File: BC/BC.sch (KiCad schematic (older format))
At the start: 32 parts, among them CON1 BARREL_JACK, Q1 Q_NMOS_GSD, Q10 Q_PMOS_GSD, Q11 Q_PMOS_GSD, Q12 Q_PMOS_GSD, Q13 Q_PMOS_GSD, Q14 Q_PMOS_GSD, Q15 Q_PMOS_GSD, Q16 Q_PMOS_GSD, Q2 Q_NMOS_GSD, Q3 Q_PMOS_GSD, Q4 Q_PMOS_GSD, Q5 Q_NMOS_GSD, Q6 Q_PMOS_GSD, Q7 Q_PMOS_GSD, Q8 Q_PMOS_GSD, Q9 Q_PMOS_GSD, SW1 SW_PUSH, U1 DS3231N, U2 MSP430G2203IPW28, U3 AP1117

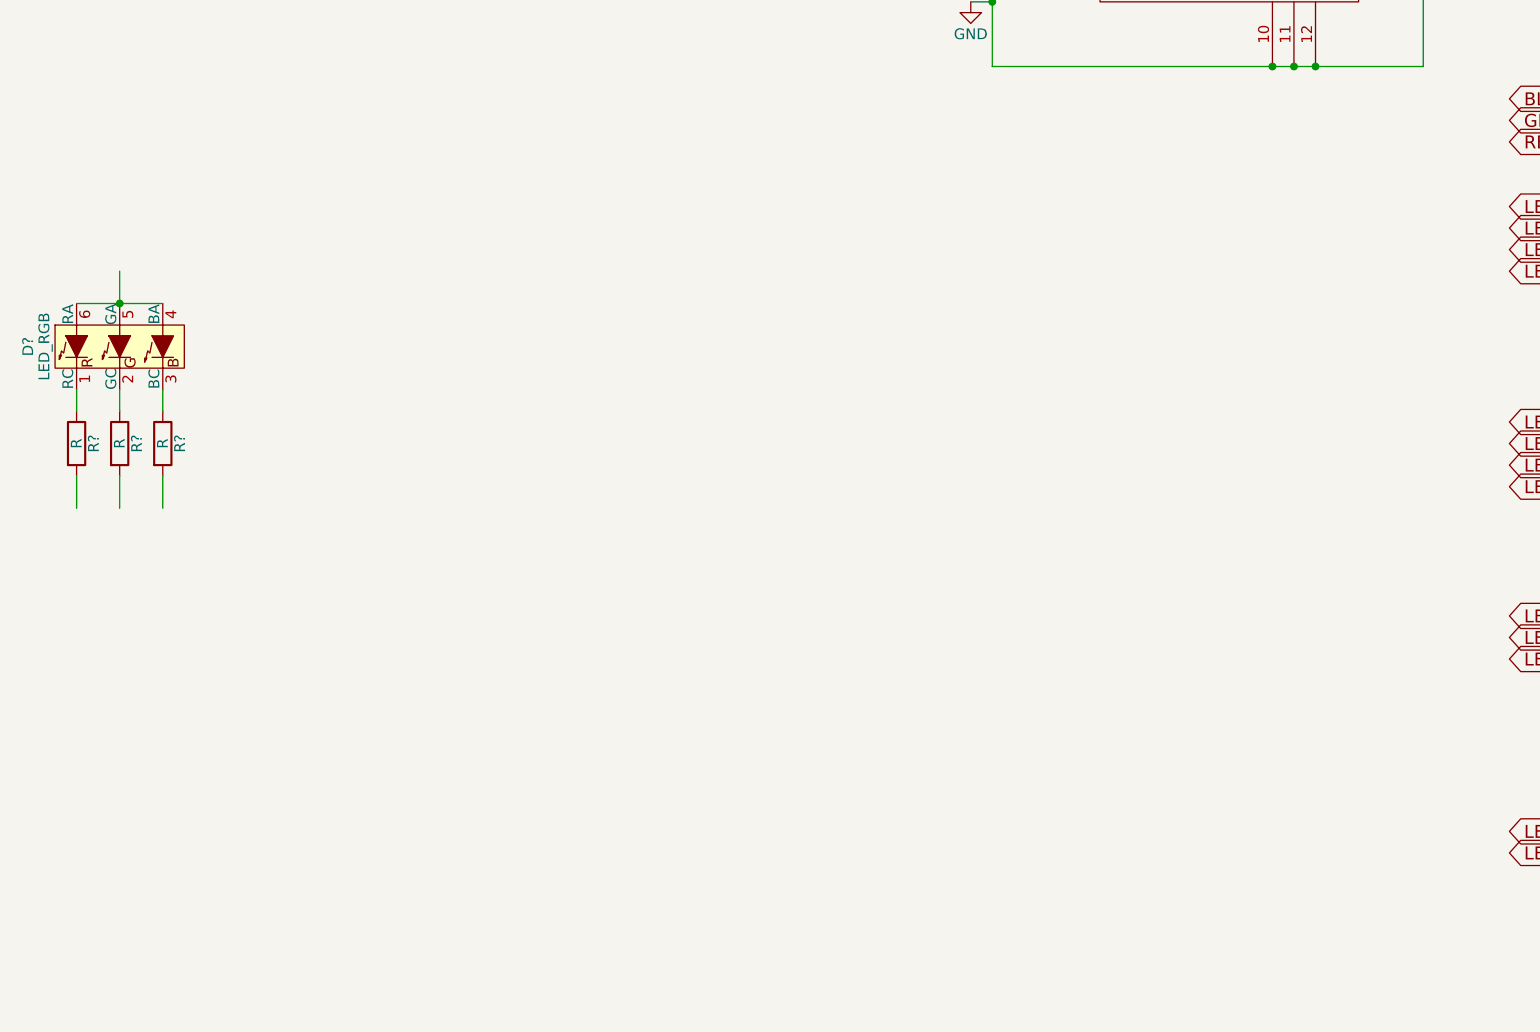
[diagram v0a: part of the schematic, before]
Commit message: Updated for 6pin RGB LED
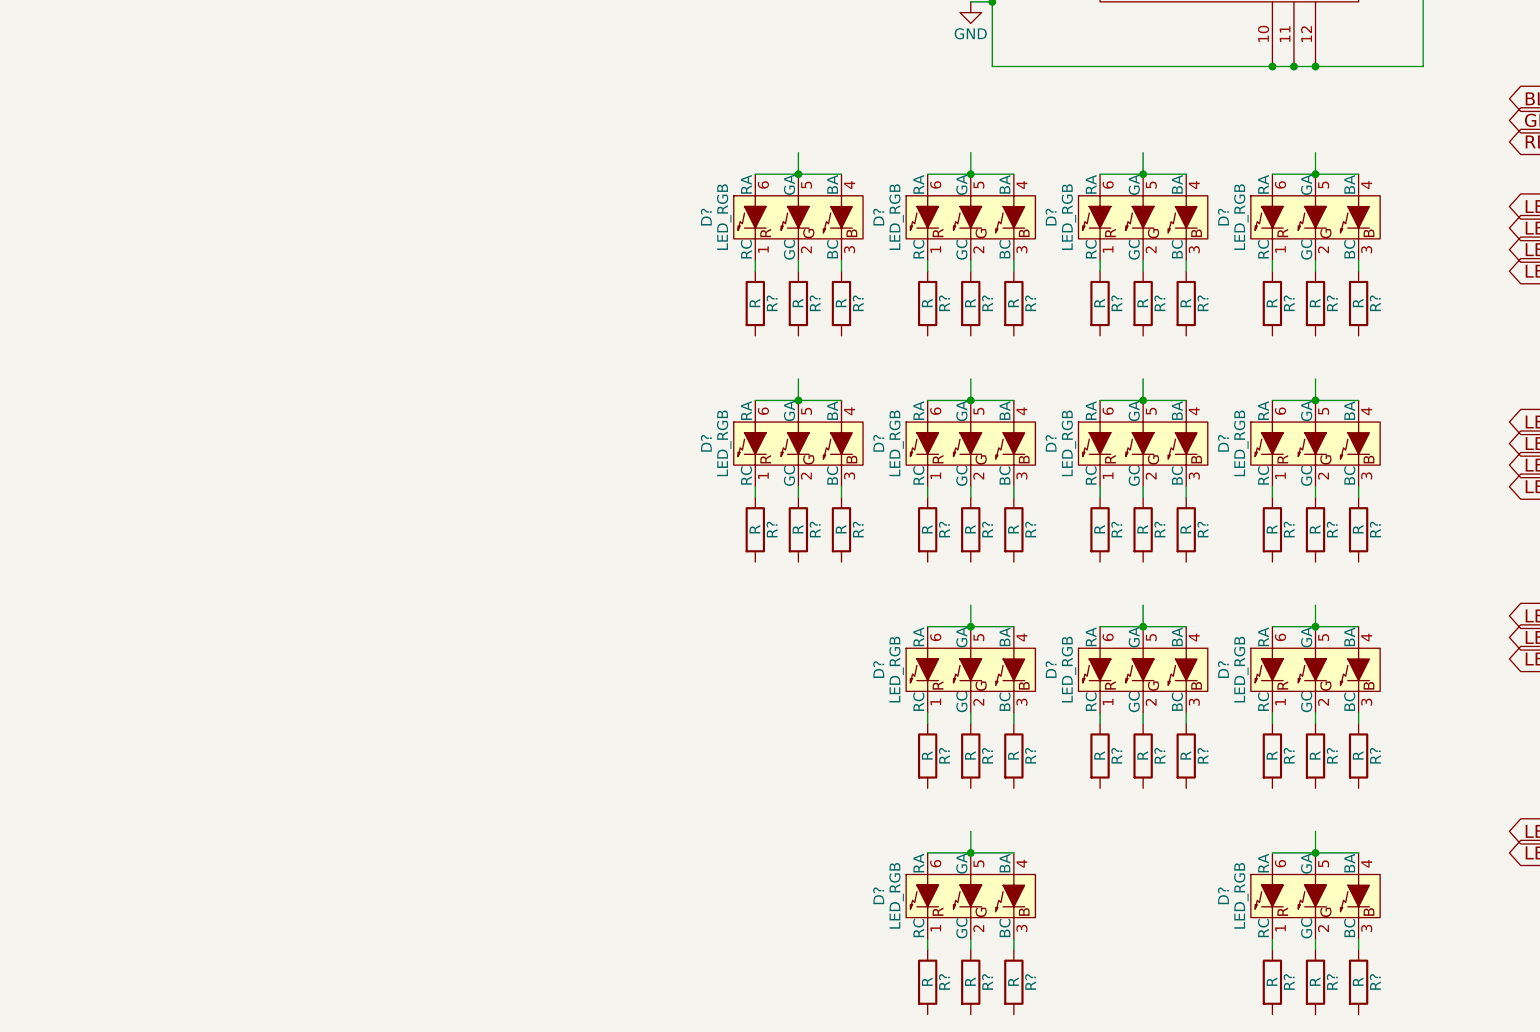
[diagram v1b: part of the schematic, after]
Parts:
- added D? (x12): LED_RGB, symbol LED_RGB
- added R? (x36): R, symbol R
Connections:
- wire segments 63 -> 120
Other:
- moved on the sheet: D?, R?

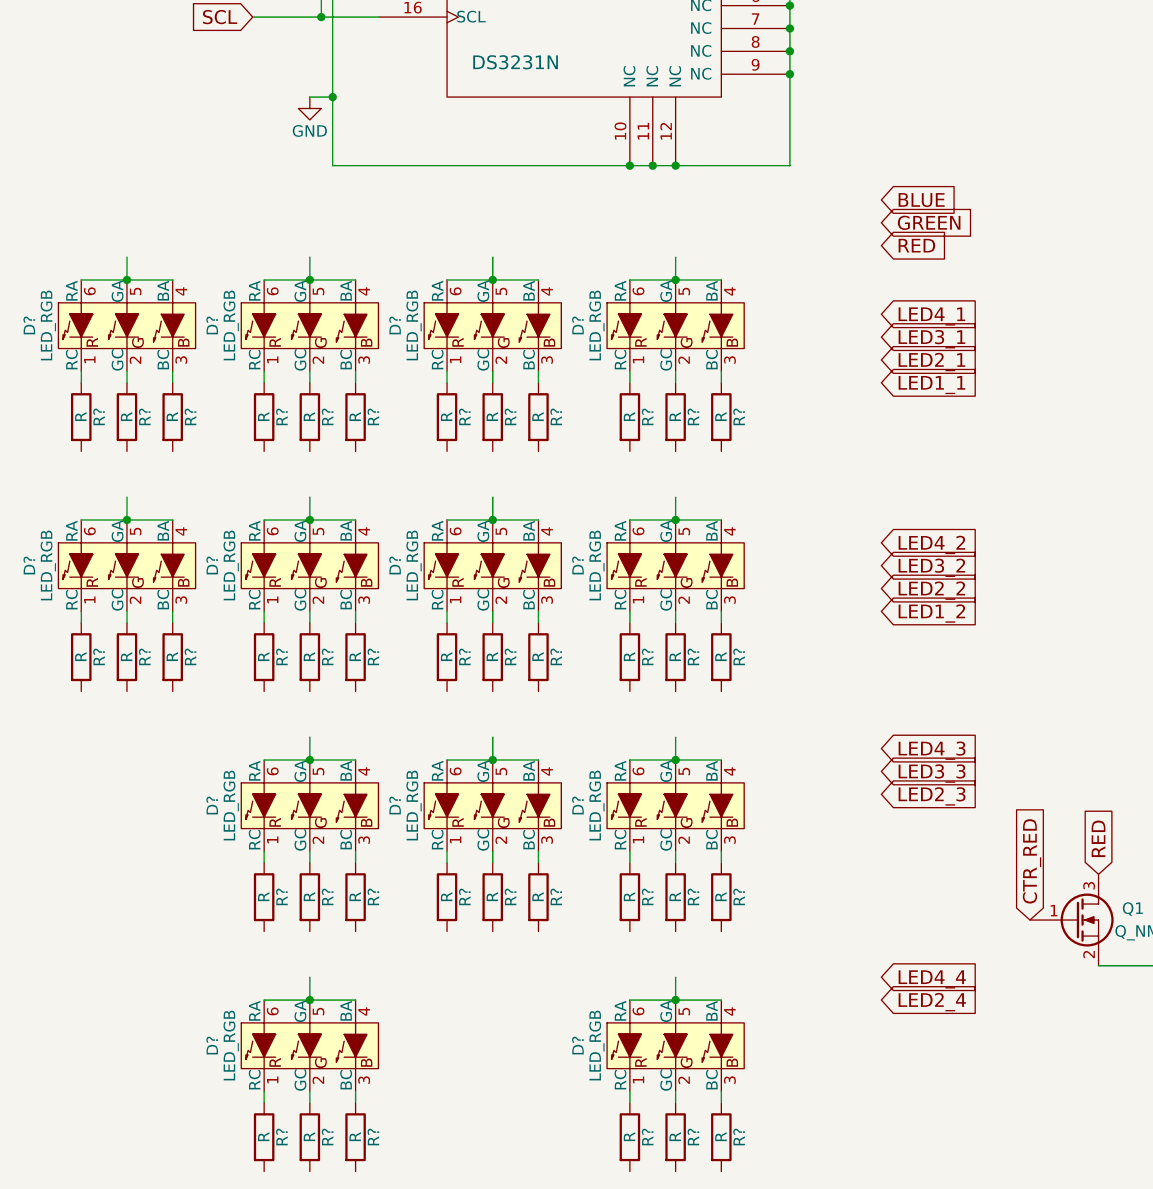
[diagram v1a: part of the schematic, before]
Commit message: Began PCB Layout
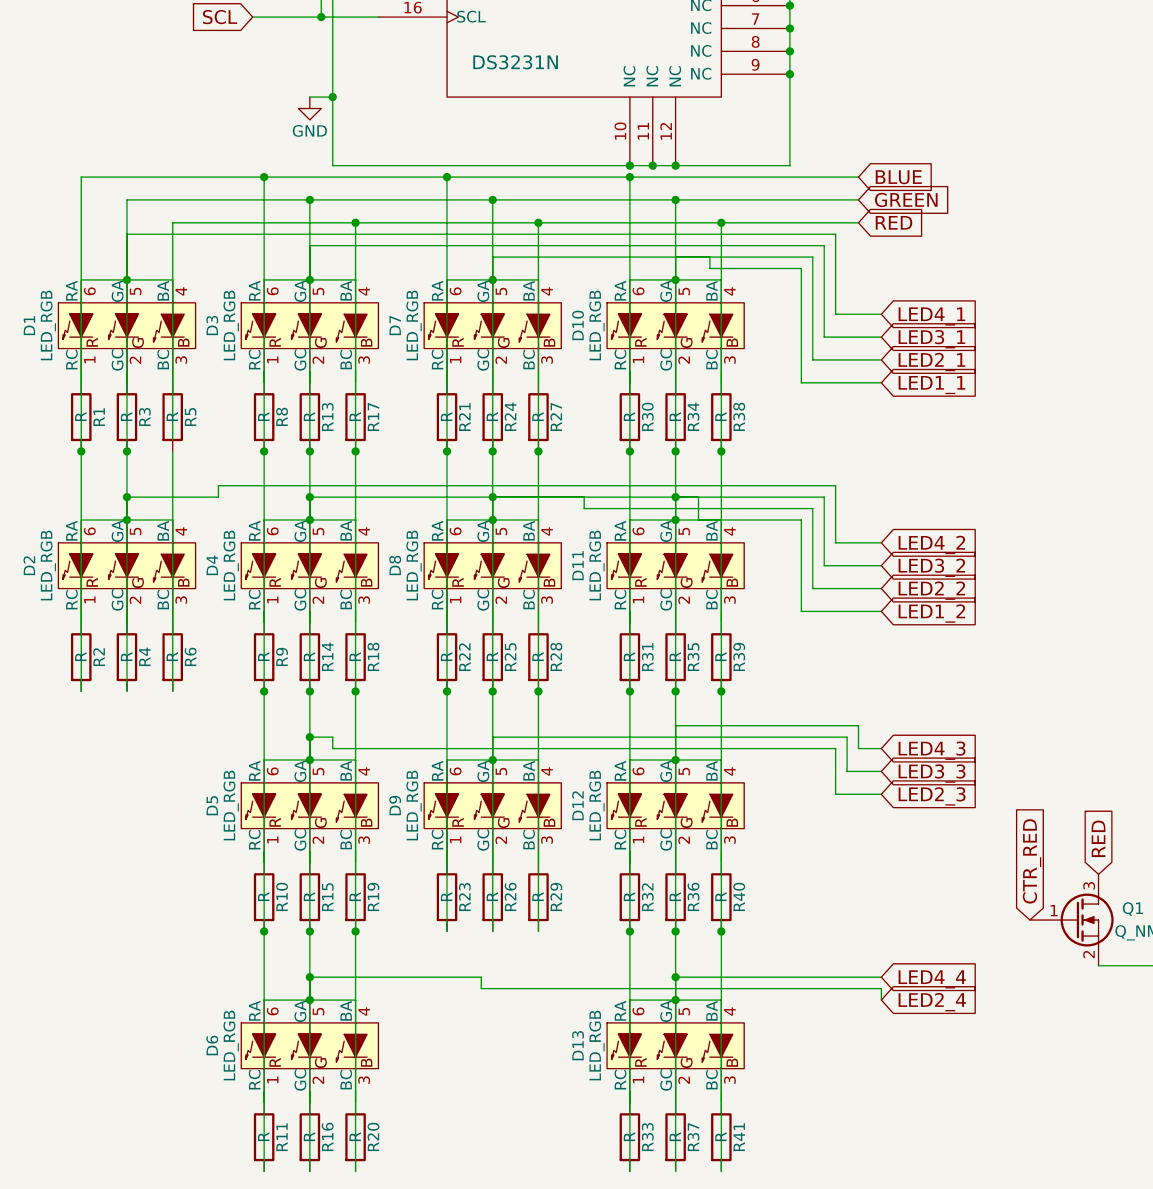
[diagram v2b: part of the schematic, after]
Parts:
- BT1: footprint (none) -> Connect:Banana_Jack_2Pin
- C1, C2, C3: footprint (none) -> Capacitors_SMD:C_0805_HandSoldering
- D1, D10, D11, D12, D13, D2, D3, D4, D5, D6, D7, D8, D9: renamed from D?; footprint (none) -> LEDs:LED_RGB_PLLC-6
- R1, R10, R11, R13, R14, R15, R16, R17, R18, R19, R2, R20, R21, R22, R23, R24, R25, R26, R27, R28, R29, R3, R30, R31, R32, R33, R34, R35, R36, R37, R38, R39, R4, R40, R41, R5, R6, R8, R9: renamed from R?; footprint (none) -> Resistors_SMD:R_0805_HandSoldering
- R12, R42, R7: footprint Resistors_SMD:R_1206_HandSoldering -> Resistors_SMD:R_0805_HandSoldering
- U1: footprint (none) -> SMD_Packages:SO-16-L
- U2: footprint (none) -> SMD_Packages:SOIC-28
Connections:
- wire segments 120 -> 184
